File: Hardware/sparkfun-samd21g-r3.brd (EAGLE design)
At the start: 57.1 x 53.3 mm, 61 parts, among them Q1 2.5A/30V, Q2 2N7002PW, U1 MCP73831, U2 74AHC1G125, U3 MIC5219 3.3V, U4 ATSAMD21G-A, Y1 32.768kHz

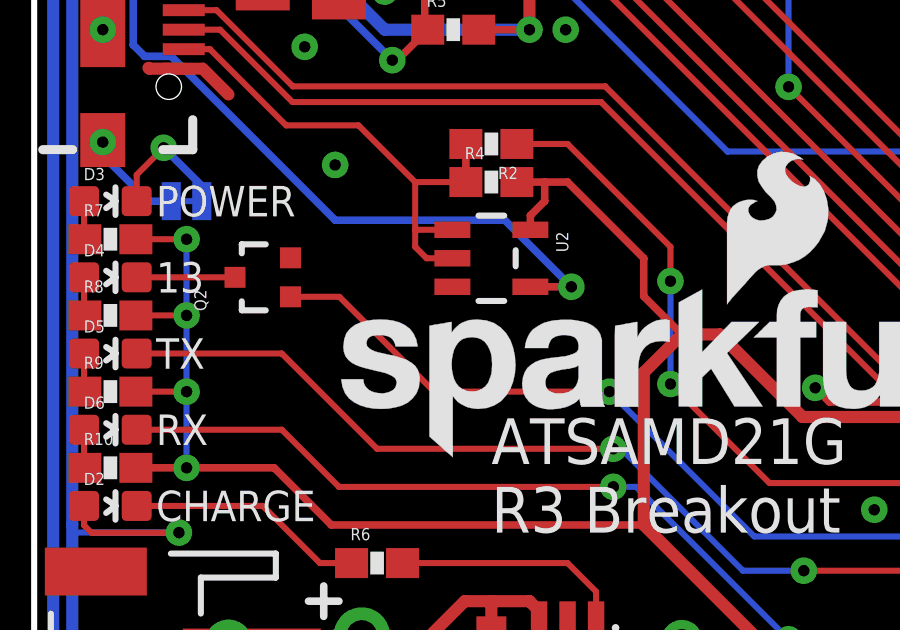
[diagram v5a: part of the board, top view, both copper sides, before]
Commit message: Adding pull-down resistor to D13 LED/MOSFET
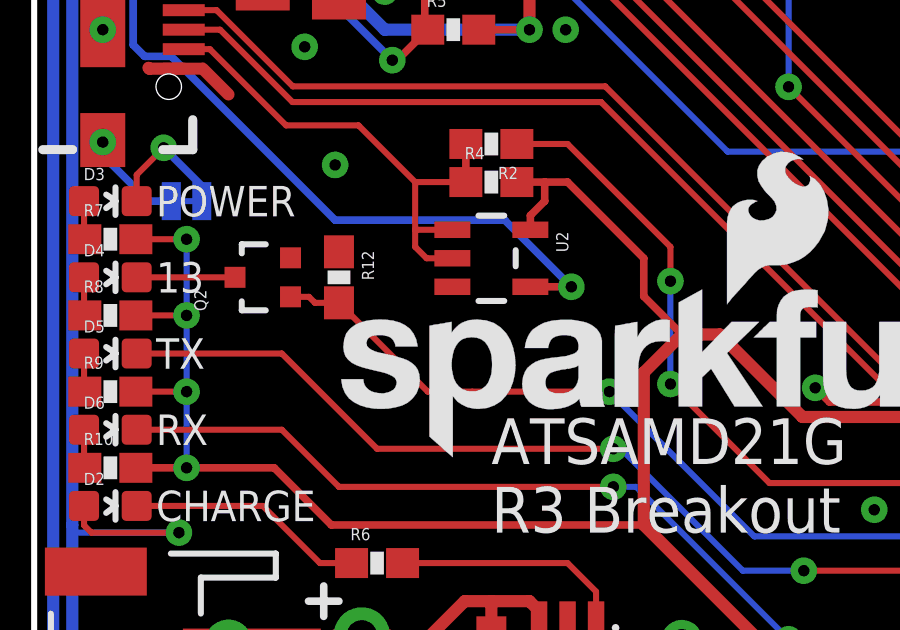
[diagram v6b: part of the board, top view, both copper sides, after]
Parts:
- added R12: 100k, SparkFun-Resistors:0603-RES
- moved LOGO4 10.8 mm to (12.7, 27.3)
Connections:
- net D13: now also R12.2
- net GND: now also R12.1
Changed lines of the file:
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@@
 <setting verticaltext="up"/>
 </settings>
-<grid distance="0.025" unitdist="inch" unit="inch" style="lines" multiple="1" display="yes" altdistance="0.005" altunitdist="inch" altunit="inch"/>
+<grid distance="0.05" unitdist="inch" unit="inch" style="lines" multiple="1" display="yes" altdistance="0.005" altunitdist="inch" altunit="inch"/>
 <layers>
 <layer number="1" name="Top" color="4" fill="1" visible="yes" active="yes"/>
@@
 <wire x1="10.922" y1="16.637" x2="10.922" y2="15.621" width="0.254" layer="22"/>
 <wire x1="51.816" y1="31.75" x2="52.578" y2="31.75" width="0.2032" layer="21"/>
+<text x="24.13" y="11.43" size="0.889" layer="22" font="vector" ratio="15" rot="MR90" align="center-left">A13</text>
+<text x="26.67" y="11.43" size="0.889" layer="22" font="vector" ratio="15" rot="MR90" align="center-left">B22</text>
+<text x="29.21" y="11.43" size="0.889" layer="22" font="vector" ratio="15" rot="MR90" align="center-left">B23</text>
+<text x="31.75" y="11.43" size="0.889" layer="22" font="vector" ratio="15" rot="MR90" align="center-left">SWCLK</text>
+<text x="34.29" y="11.43" size="0.889" layer="22" font="vector" ratio="15" rot="MR90" align="center-left">SWDIO</text>
 </plain>
 <attributes>
@@
 <element name="JP5" library="SparkFun-Connectors" package="1X05_NO_SILK" value="" x="34.29" y="10.16" rot="R180"/>
 <element name="LOGO2" library="SparkFun-Aesthetics" package="SFE_LOGO_NAME_FLAME_.4" value="SFE_LOGO_NAME_FLAME.4_INCH" x="50.8" y="7.62" rot="MR45"/>
-<element name="LOGO4" library="SparkFun-Aesthetics" package="OSHW-LOGO-L" value="OSHW-LOGOL" x="17.78" y="36.83" rot="MR0"/>
+<element name="LOGO4" library="SparkFun-Aesthetics" package="OSHW-LOGO-L" value="OSHW-LOGOL" x="12.7" y="27.305" rot="MR0"/>
 <element name="D1" library="SparkFun-DiscreteSemi" package="SOD-323" value="BAT20J" x="12.7" y="19.05" rot="R90">
 <attribute name="PROD_ID" value="DIO-11623" x="12.7" y="19.05" size="0.889" layer="27" font="vector" ratio="15" rot="R90" display="off"/>
@@
 <element name="JP8" library="SparkFun-Connectors" package="JST-2-PTH-NS" value="" x="6.477" y="19.177" rot="R90"/>
 <element name="JP9" library="SparkFun-Connectors" package="1X02_NO_SILK" value="" x="10.922" y="17.907" rot="R90"/>
+<element name="R12" library="SparkFun-Resistors" package="0603-RES" value="100k" x="10.16" y="32.385" rot="R270">
+<attribute name="PROD_ID" value="RES-07828" x="10.16" y="32.385" size="1.778" layer="27" font="vector" ratio="15" rot="R270" display="off"/>
+</element>
 </elements>
 <signals>
@@
 <wire x1="42.35" y1="29.73" x2="41.39" y2="29.73" width="0.254" layer="1"/>
 <wire x1="41.39" y1="29.73" x2="40.64" y2="30.48" width="0.254" layer="1"/>
+<contactref element="R12" pad="1"/>
 </signal>
 <signal name="3.3V">
@@
 <via x="19.177" y="28.575" extent="1-16" drill="0.381"/>
 <wire x1="8.56" y1="31.75" x2="8.545" y2="31.735" width="0.2032" layer="1"/>
-<wire x1="19.177" y1="28.575" x2="13.335" y2="28.575" width="0.2032" layer="1"/>
-<wire x1="13.335" y1="28.575" x2="10.175" y2="31.735" width="0.2032" layer="1"/>
-<wire x1="10.175" y1="31.735" x2="8.545" y2="31.735" width="0.2032" layer="1"/>
+<wire x1="19.177" y1="28.575" x2="14.605" y2="28.575" width="0.2032" layer="1"/>
 <wire x1="35.687" y1="30.353" x2="35.687" y2="31.623" width="0.2032" layer="16"/>
 <wire x1="35.687" y1="31.623" x2="35.306" y2="32.004" width="0.2032" layer="16"/>
@@
 <wire x1="36.068" y1="29.083" x2="36.068" y2="29.972" width="0.2032" layer="16"/>
 <wire x1="36.068" y1="29.972" x2="35.687" y2="30.353" width="0.2032" layer="16"/>
+<contactref element="R12" pad="2"/>
+<wire x1="14.605" y1="28.575" x2="13.12" y2="28.575" width="0.2032" layer="1"/>
+<wire x1="13.12" y1="28.575" x2="10.16" y2="31.535" width="0.2032" layer="1"/>
+<wire x1="10.16" y1="31.535" x2="9.359" y2="31.535" width="0.2032" layer="1"/>
+<wire x1="8.545" y1="31.735" x2="9.159" y2="31.735" width="0.2032" layer="1"/>
+<wire x1="9.159" y1="31.735" x2="9.359" y2="31.535" width="0.2032" layer="1"/>
 </signal>
 <signal name="PA13">

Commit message: Upping version number to v10
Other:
- board text added: "v10"
- board text removed: "v01"
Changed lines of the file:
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@@
 <grid distance="0.05" unitdist="inch" unit="inch" style="lines" multiple="1" display="yes" altdistance="0.005" altunitdist="inch" altunit="inch"/>
 <layers>
-<layer number="1" name="Top" color="4" fill="1" visible="yes" active="yes"/>
+<layer number="1" name="Top" color="4" fill="1" visible="no" active="yes"/>
 <layer number="2" name="Route2" color="1" fill="3" visible="no" active="no"/>
 <layer number="3" name="Route3" color="4" fill="3" visible="no" active="no"/>
@@
 <layer number="19" name="Unrouted" color="6" fill="1" visible="yes" active="yes"/>
 <layer number="20" name="Dimension" color="15" fill="1" visible="yes" active="yes"/>
-<layer number="21" name="tPlace" color="16" fill="1" visible="yes" active="yes"/>
+<layer number="21" name="tPlace" color="16" fill="1" visible="no" active="yes"/>
 <layer number="22" name="bPlace" color="14" fill="1" visible="yes" active="yes"/>
-<layer number="23" name="tOrigins" color="15" fill="1" visible="yes" active="yes"/>
+<layer number="23" name="tOrigins" color="15" fill="1" visible="no" active="yes"/>
 <layer number="24" name="bOrigins" color="15" fill="1" visible="yes" active="yes"/>
 <layer number="25" name="tNames" color="7" fill="1" visible="no" active="yes"/>
@@
 <layer number="49" name="Reference" color="7" fill="1" visible="no" active="yes"/>
 <layer number="50" name="dxf" color="7" fill="1" visible="no" active="no"/>
-<layer number="51" name="tDocu" color="6" fill="1" visible="yes" active="yes"/>
-<layer number="52" name="bDocu" color="6" fill="1" visible="no" active="yes"/>
+<layer number="51" name="tDocu" color="6" fill="1" visible="no" active="yes"/>
+<layer number="52" name="bDocu" color="6" fill="1" visible="yes" active="yes"/>
 <layer number="53" name="tGND_GNDA" color="7" fill="9" visible="no" active="no"/>
 <layer number="54" name="bGND_GNDA" color="1" fill="9" visible="no" active="no"/>
@@
 <text x="7.366" y="49.53" size="1.27" layer="21" font="vector" ratio="15" rot="R90" align="center-right">SCL</text>
 <text x="54.991" y="16.51" size="1.27" layer="21" font="vector" ratio="15" rot="R90" align="top-center">RESET</text>
-<text x="3.81" y="48.26" size="1.016" layer="16" font="vector" ratio="15" rot="MR0" align="top-center">v01</text>
+<text x="3.81" y="48.26" size="1.016" layer="16" font="vector" ratio="15" rot="MR0" align="top-center">v10</text>
 <text x="55.88" y="30.734" size="0.889" layer="21" font="vector" ratio="15" rot="R270" align="bottom-center">3V3</text>
 <text x="51.308" y="30.48" size="0.889" layer="21" font="vector" ratio="15" align="center-right">MISO</text>

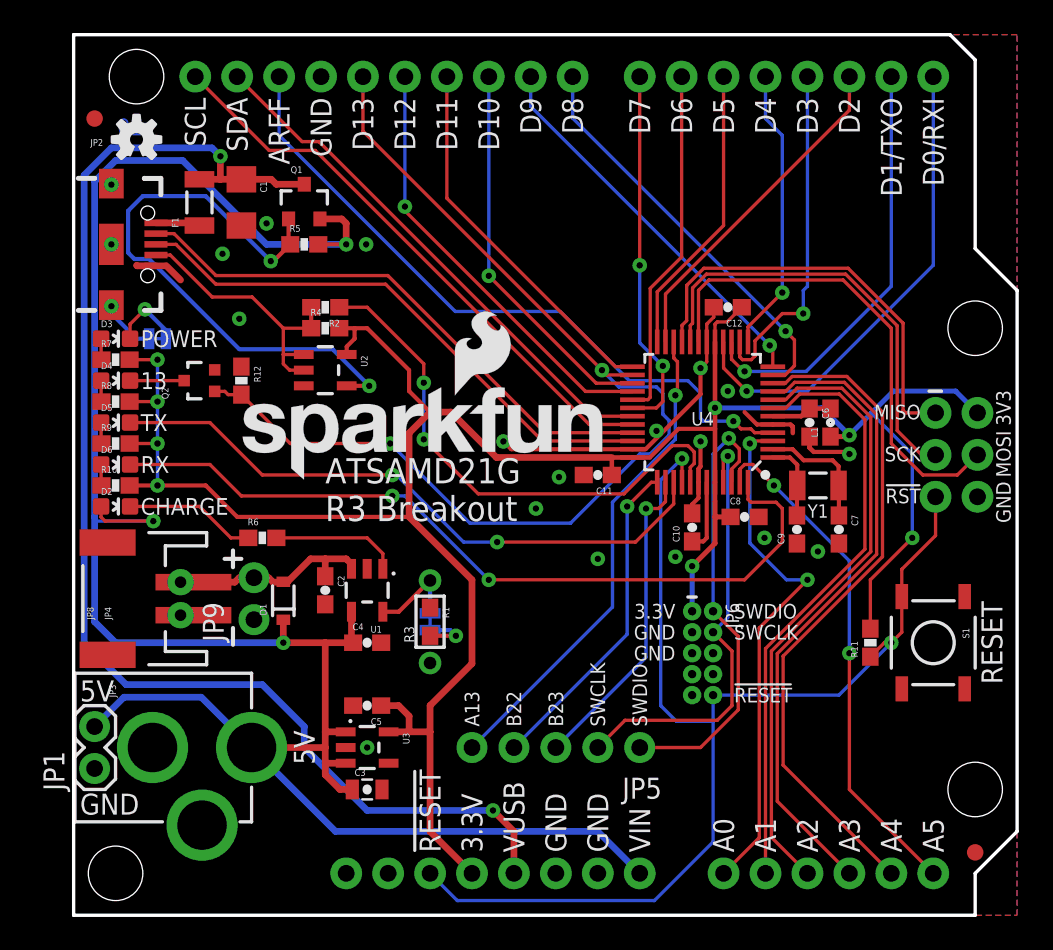
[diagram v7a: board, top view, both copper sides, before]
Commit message: Pulling buffer up to VIN instead of 3.3V
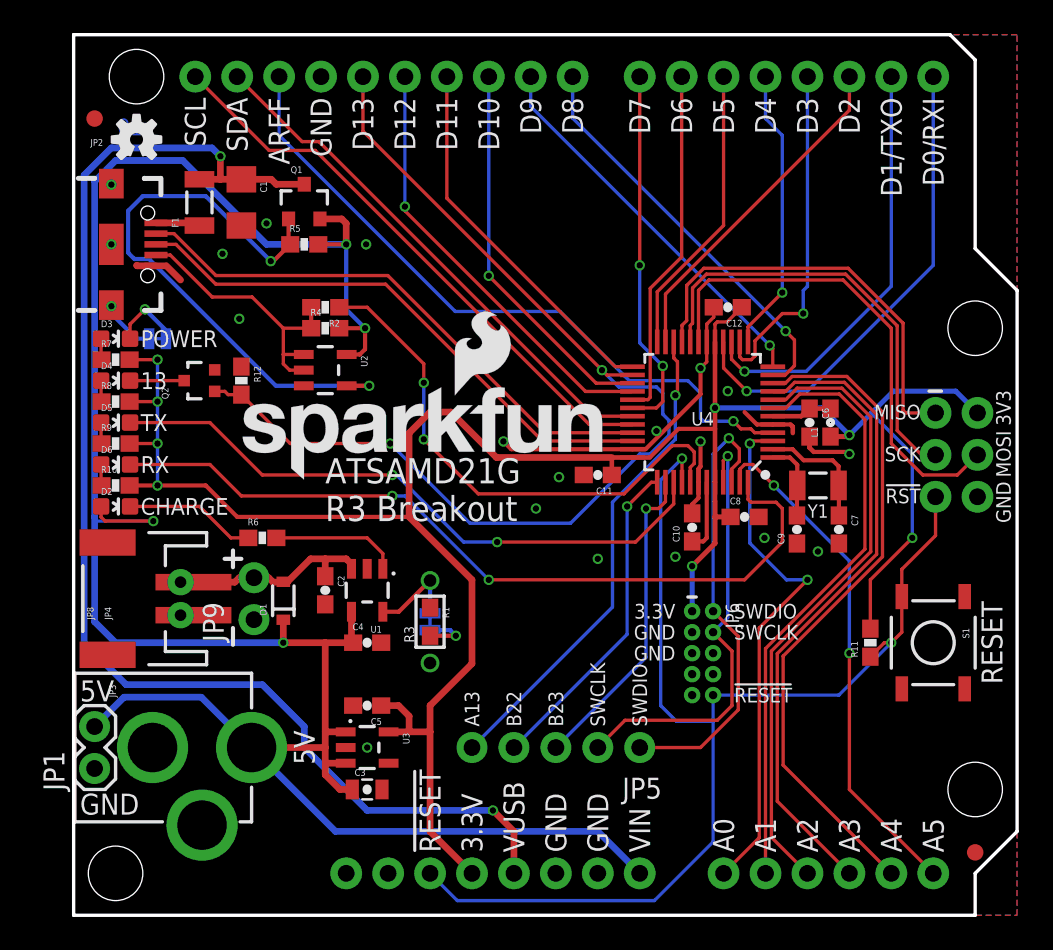
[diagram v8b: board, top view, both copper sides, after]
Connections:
- net 3.3V: no longer R4.2, U2.5
- net VIN: now also R4.2, U2.5
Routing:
- net 3.3V: track 153.8 -> 143.7 mm
- net VIN: track 131.5 -> 141.2 mm, vias 3 -> 4
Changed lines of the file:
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@@
 <grid distance="0.05" unitdist="inch" unit="inch" style="lines" multiple="1" display="yes" altdistance="0.005" altunitdist="inch" altunit="inch"/>
 <layers>
-<layer number="1" name="Top" color="4" fill="1" visible="no" active="yes"/>
+<layer number="1" name="Top" color="4" fill="1" visible="yes" active="yes"/>
 <layer number="2" name="Route2" color="1" fill="3" visible="no" active="no"/>
 <layer number="3" name="Route3" color="4" fill="3" visible="no" active="no"/>
@@
 <layer number="19" name="Unrouted" color="6" fill="1" visible="yes" active="yes"/>
 <layer number="20" name="Dimension" color="15" fill="1" visible="yes" active="yes"/>
-<layer number="21" name="tPlace" color="16" fill="1" visible="no" active="yes"/>
+<layer number="21" name="tPlace" color="16" fill="1" visible="yes" active="yes"/>
 <layer number="22" name="bPlace" color="14" fill="1" visible="yes" active="yes"/>
-<layer number="23" name="tOrigins" color="15" fill="1" visible="no" active="yes"/>
+<layer number="23" name="tOrigins" color="15" fill="1" visible="yes" active="yes"/>
 <layer number="24" name="bOrigins" color="15" fill="1" visible="yes" active="yes"/>
 <layer number="25" name="tNames" color="7" fill="1" visible="no" active="yes"/>
@@
 <layer number="47" name="Measures" color="7" fill="1" visible="no" active="yes"/>
 <layer number="48" name="Document" color="7" fill="1" visible="no" active="yes"/>
-<layer number="49" name="Reference" color="7" fill="1" visible="no" active="yes"/>
+<layer number="49" name="Reference" color="7" fill="1" visible="yes" active="yes"/>
 <layer number="50" name="dxf" color="7" fill="1" visible="no" active="no"/>
-<layer number="51" name="tDocu" color="6" fill="1" visible="no" active="yes"/>
-<layer number="52" name="bDocu" color="6" fill="1" visible="yes" active="yes"/>
+<layer number="51" name="tDocu" color="6" fill="1" visible="yes" active="yes"/>
+<layer number="52" name="bDocu" color="6" fill="1" visible="no" active="yes"/>
 <layer number="53" name="tGND_GNDA" color="7" fill="9" visible="no" active="no"/>
 <layer number="54" name="bGND_GNDA" color="1" fill="9" visible="no" active="no"/>
@@
 </class>
 </classes>
-<designrules name="SparkFun-2-layer *">
+<designrules name="Gold_Phoenix_Standard_Spec_2_layer">
 <description language="en">&lt;b&gt;EAGLE Design Rules&lt;/b&gt;
 &lt;p&gt;
@@
 <param name="mtCopper" value="0.035mm 0.035mm 0.035mm 0.035mm 0.035mm 0.035mm 0.035mm 0.035mm 0.035mm 0.035mm 0.035mm 0.035mm 0.035mm 0.035mm 0.035mm 0.035mm"/>
 <param name="mtIsolate" value="1.5mm 0.15mm 0.2mm 0.15mm 0.2mm 0.15mm 0.2mm 0.15mm 0.2mm 0.15mm 0.2mm 0.15mm 0.2mm 0.15mm 0.2mm"/>
-<param name="mdWireWire" value="6mil"/>
-<param name="mdWirePad" value="6mil"/>
-<param name="mdWireVia" value="6mil"/>
-<param name="mdPadPad" value="6mil"/>
-<param name="mdPadVia" value="6mil"/>
-<param name="mdViaVia" value="6mil"/>
-<param name="mdSmdPad" value="6mil"/>
-<param name="mdSmdVia" value="6mil"/>
-<param name="mdSmdSmd" value="6mil"/>
+<param name="mdWireWire" value="5mil"/>
+<param name="mdWirePad" value="5mil"/>
+<param name="mdWireVia" value="5mil"/>
+<param name="mdPadPad" value="5mil"/>
+<param name="mdPadVia" value="5mil"/>
+<param name="mdViaVia" value="5mil"/>
+<param name="mdSmdPad" value="5mil"/>
+<param name="mdSmdVia" value="5mil"/>
+<param name="mdSmdSmd" value="5mil"/>
 <param name="mdViaViaSameLayer" value="8mil"/>
 <param name="mnLayersViaInSmd" value="2"/>
@@
 <param name="mdDrill" value="8mil"/>
 <param name="mdSmdStop" value="0mil"/>
-<param name="msWidth" value="7mil"/>
-<param name="msDrill" value="15mil"/>
+<param name="msWidth" value="5mil"/>
+<param name="msDrill" value="6mil"/>
 <param name="msMicroVia" value="9.99mm"/>
 <param name="msBlindViaRatio" value="0.5"/>
@@
 <param name="rvMicroViaOuter" value="0.25"/>
 <param name="rvMicroViaInner" value="0.25"/>
-<param name="rlMinPadTop" value="12mil"/>
+<param name="rlMinPadTop" value="5mil"/>
 <param name="rlMaxPadTop" value="20mil"/>
 <param name="rlMinPadInner" value="10mil"/>
 <param name="rlMaxPadInner" value="20mil"/>
-<param name="rlMinPadBottom" value="12mil"/>
+<param name="rlMinPadBottom" value="5mil"/>
 <param name="rlMaxPadBottom" value="20mil"/>
-<param name="rlMinViaOuter" value="10mil"/>
+<param name="rlMinViaOuter" value="5mil"/>
 <param name="rlMaxViaOuter" value="20mil"/>
 <param name="rlMinViaInner" value="10mil"/>
@@
 <contactref element="R8" pad="2"/>
 <contactref element="JP6" pad="1"/>
-<contactref element="R4" pad="2"/>
-<contactref element="U2" pad="5"/>
 <contactref element="R9" pad="2"/>
 <contactref element="R10" pad="2"/>
@@
 <wire x1="39.585" y1="35.941" x2="40.474" y2="36.83" width="0.2032" layer="1"/>
 <via x="46.99" y="29.083" extent="1-16" drill="0.381"/>
-<wire x1="16.09" y1="35.56" x2="17.018" y2="35.56" width="0.254" layer="1"/>
-<wire x1="17.018" y1="35.56" x2="17.78" y2="35.56" width="0.254" layer="1"/>
-<wire x1="16.5401" y1="33.97" x2="16.5401" y2="34.4471" width="0.254" layer="1"/>
-<wire x1="16.5401" y1="34.4471" x2="17.018" y2="34.925" width="0.254" layer="1"/>
-<wire x1="17.018" y1="34.925" x2="17.018" y2="35.56" width="0.254" layer="1"/>
 <via x="38.85" y="30.734" extent="1-16" drill="0.381"/>
 <wire x1="38.85" y1="30.734" x2="45.339" y2="30.734" width="0.3048" layer="16"/>
@@
 <wire x1="22.86" y1="30.48" x2="25.61" y2="27.73" width="0.4064" layer="1"/>
 <wire x1="9.906" y1="24.13" x2="20.32" y2="24.13" width="0.254" layer="1"/>
-<wire x1="21.59" y1="30.48" x2="20.32" y2="31.75" width="0.254" layer="1"/>
-<wire x1="20.32" y1="31.75" x2="20.32" y2="33.02" width="0.254" layer="1"/>
-<wire x1="20.32" y1="33.02" x2="17.78" y2="35.56" width="0.254" layer="1"/>
 <wire x1="20.32" y1="24.13" x2="24.13" y2="20.32" width="0.4064" layer="1"/>
 <wire x1="19.0801" y1="11.11" x2="20.32" y2="11.11" width="0.4064" layer="1"/>
@@
 <wire x1="1.663" y1="24.118" x2="1.905" y2="23.876" width="0.2032" layer="1"/>
 <wire x1="1.905" y1="23.876" x2="4.826" y2="23.876" width="0.2032" layer="1"/>
+<contactref element="R4" pad="2"/>
+<contactref element="U2" pad="5"/>
+<wire x1="16.5401" y1="33.97" x2="17.333" y2="33.97" width="0.254" layer="1"/>
+<wire x1="17.333" y1="33.97" x2="17.653" y2="34.29" width="0.254" layer="1"/>
+<wire x1="17.653" y1="34.29" x2="17.653" y2="35.56" width="0.254" layer="1"/>
+<via x="17.653" y="35.56" extent="1-16" drill="0.381"/>
+<wire x1="17.653" y1="35.56" x2="16.51" y2="36.703" width="0.254" layer="16"/>
+<wire x1="16.51" y1="36.703" x2="16.51" y2="40.64" width="0.254" layer="16"/>
+<wire x1="16.09" y1="35.56" x2="17.653" y2="35.56" width="0.254" layer="1"/>
 </signal>
 <signal name="A3">
@@
 <wire x1="4.191" y1="43.561" x2="8.001" y2="43.561" width="0.254" layer="16"/>
 <wire x1="8.001" y1="43.561" x2="11.938" y2="39.624" width="0.254" layer="16"/>
-<wire x1="10.033" y1="34.29" x2="15.687" y2="34.29" width="0.254" layer="16"/>
-<wire x1="15.687" y1="34.29" x2="17.907" y2="32.07" width="0.254" layer="16"/>
 <wire x1="3.302" y1="42.672" x2="3.302" y2="40.132" width="0.254" layer="16"/>
 <wire x1="3.302" y1="40.132" x2="3.683" y2="39.751" width="0.254" layer="16"/>
 <wire x1="3.683" y1="39.751" x2="4.572" y2="39.751" width="0.254" layer="16"/>
-<wire x1="4.572" y1="39.751" x2="10.033" y2="34.29" width="0.254" layer="16"/>
+<wire x1="4.572" y1="39.751" x2="12.253" y2="32.07" width="0.254" layer="16"/>
+<wire x1="12.253" y1="32.07" x2="17.907" y2="32.07" width="0.254" layer="16"/>
 </signal>
 <signal name="RX_LED">
